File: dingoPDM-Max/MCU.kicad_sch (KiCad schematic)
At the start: 29 parts, among them J5 TC, SW1 BOOT, U3 PCA82C250, U4 STM32F446RETx, Y1 8mHz

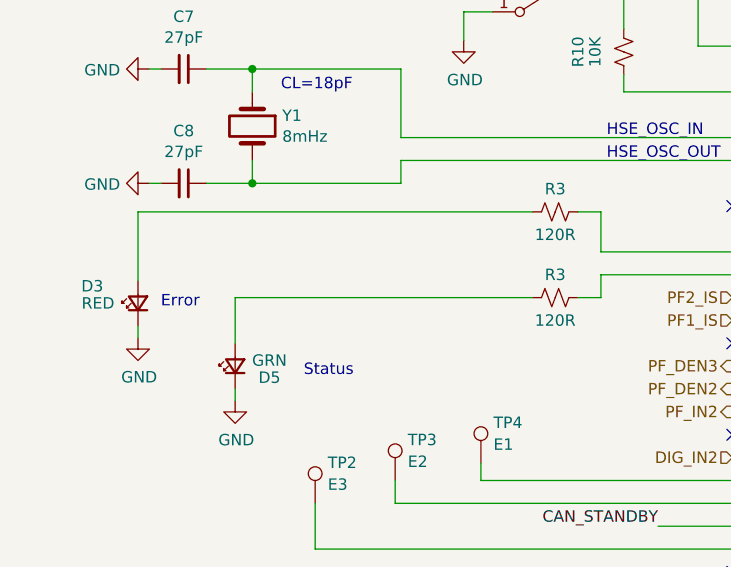
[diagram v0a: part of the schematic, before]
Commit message: Updated to Kicad 8
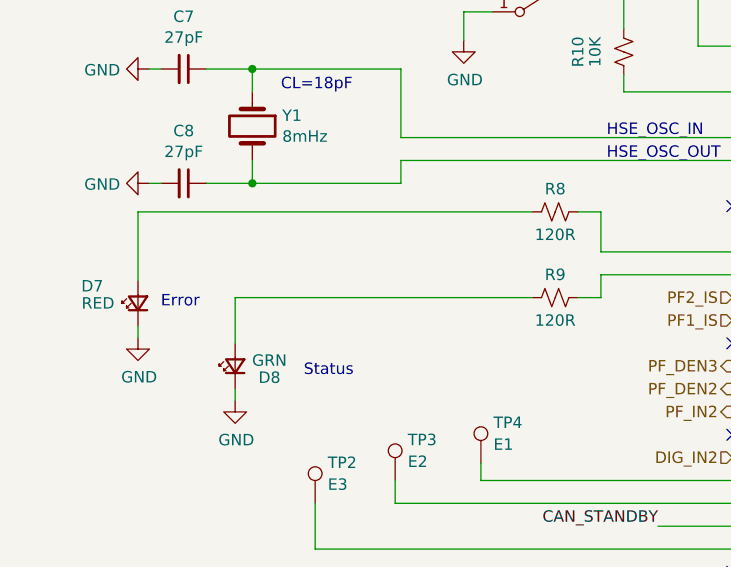
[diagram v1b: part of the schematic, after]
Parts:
- renumbered D3 to D7, D5 to D8, R3 to R8, R3 to R9
